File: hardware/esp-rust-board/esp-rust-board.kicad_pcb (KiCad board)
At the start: 2 copper layers, 22.9 x 63.5 mm, 81 parts, among them J1 USB4105-GF-A, J2 MOTOR L, J3 MOTOR R, J4 LED L, J7 SERVO R, J8 SERVO R, Q1 DMG3415U, Q2 Si2319CDS, Q3 Si2319CDS, Q4 MMBT3904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

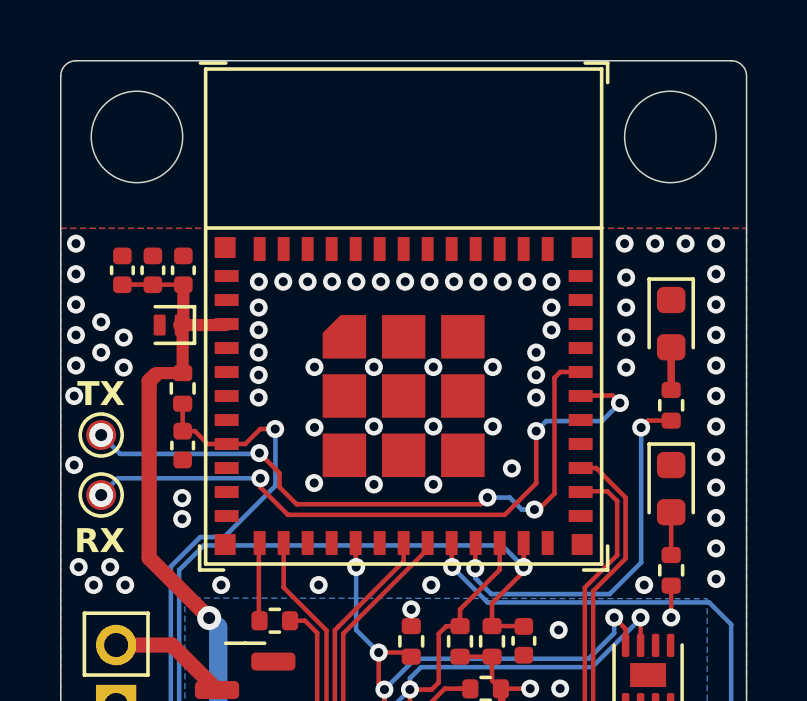
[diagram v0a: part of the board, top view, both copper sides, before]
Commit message: Remove unused rust board
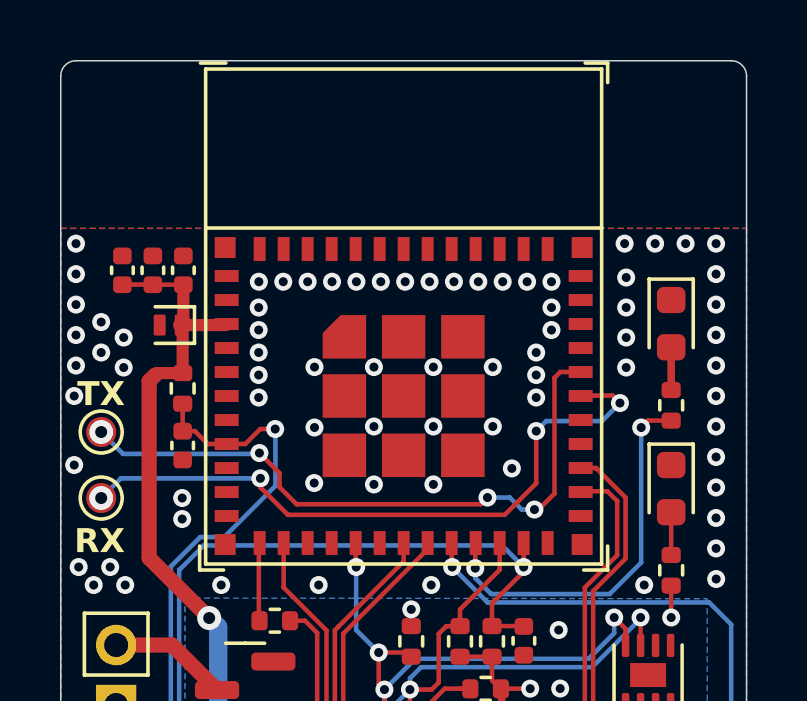
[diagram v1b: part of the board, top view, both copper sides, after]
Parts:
- removed U4: Rust_Board, Rust_Board:Rust_Board
- moved TP1 0.10 mm to (138.0, 77.4)
- moved TP3 0.10 mm to (138.0, 79.6)
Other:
- outline, holes or cut-outs redrawn
